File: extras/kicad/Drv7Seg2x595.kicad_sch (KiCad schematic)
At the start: 33 parts, among them IC1 74HC595, IC2 74HC595, J1 INTERFACE, J2 PWR_LED_JMP, Q1 MMBT3904, Q2 MMBT3904, Q3 MMBT3904, Q4 MMBT3904

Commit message: Update KiCAD files.
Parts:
- DISPLAY1: footprint Display_7Segment:CA56-12EWA -> Drv7Seg2x595:display_7seg_4d_0.56in
- J1: footprint Connector_PinHeader_2.54mm:PinHeader_1x05_P2.54mm_Horizontal -> Drv7Seg2x595:PinHeader_1x05_P2.54mm_Horizontal
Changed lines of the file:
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@@
 	)
 	(symbol
+		(lib_name "MountingHole_3")
 		(lib_id "Mechanical:MountingHole")
 		(at 234.95 102.87 0)
@@
 			)
 		)
-		(property "Footprint" "Display_7Segment:CA56-12EWA"
+		(property "Footprint" "Drv7Seg2x595:display_7seg_4d_0.56in"
 			(at 112.522 96.52 0)
 			(effects
@@
 			)
 		)
-		(property "Footprint" "Connector_PinHeader_2.54mm:PinHeader_1x05_P2.54mm_Horizontal"
+		(property "Footprint" "Drv7Seg2x595:PinHeader_1x05_P2.54mm_Horizontal"
 			(at 196.342 80.772 0)
 			(effects
@@
 	)
 	(symbol
+		(lib_name "MountingHole_2")
 		(lib_id "Mechanical:MountingHole")
 		(at 234.95 90.17 0)
@@
 	)
 	(symbol
+		(lib_name "MountingHole_1")
 		(lib_id "Mechanical:MountingHole")
 		(at 234.95 109.22 0)

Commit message: Add SOT-23 to project-wide library for portability.
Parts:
- Q3, Q4: footprint Package_TO_SOT_SMD:SOT-23 -> Drv7Seg2x595:SOT-23
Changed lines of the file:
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@@
 			)
 		)
-		(property "Footprint" "Package_TO_SOT_SMD:SOT-23"
+		(property "Footprint" "Drv7Seg2x595:SOT-23"
 			(at 128.27 95.885 0)
 			(effects
@@
 			)
 		)
-		(property "Footprint" "Package_TO_SOT_SMD:SOT-23"
+		(property "Footprint" "Drv7Seg2x595:SOT-23"
 			(at 116.84 104.775 0)
 			(effects

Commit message: Update symbol for transistors.
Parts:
- Q1, Q2: footprint Package_TO_SOT_SMD:SOT-23 -> Drv7Seg2x595:SOT-23; symbol Transistor_BJT:MMBT3904 -> Drv7Seg2x595:MMBT3904
- Q3, Q4: symbol Transistor_BJT:MMBT3904 -> Drv7Seg2x595:MMBT3904
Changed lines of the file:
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@@
 	)
 	(symbol
-		(lib_name "MMBT3904_1")
-		(lib_id "Transistor_BJT:MMBT3904")
+		(lib_id "Drv7Seg2x595:MMBT3904")
 		(at 133.35 93.98 0)
 		(mirror y)
@@
 	)
 	(symbol
-		(lib_id "Transistor_BJT:MMBT3904")
+		(lib_id "Drv7Seg2x595:MMBT3904")
 		(at 110.49 111.76 0)
 		(mirror y)
@@
 			)
 		)
-		(property "Footprint" "Package_TO_SOT_SMD:SOT-23"
+		(property "Footprint" "Drv7Seg2x595:SOT-23"
 			(at 105.41 113.665 0)
 			(effects
@@
 	)
 	(symbol
-		(lib_id "Transistor_BJT:MMBT3904")
+		(lib_id "Drv7Seg2x595:MMBT3904")
 		(at 99.06 120.65 0)
 		(mirror y)
@@
 			)
 		)
-		(property "Footprint" "Package_TO_SOT_SMD:SOT-23"
+		(property "Footprint" "Drv7Seg2x595:SOT-23"
 			(at 93.98 122.555 0)
 			(effects
@@
 	)
 	(symbol
-		(lib_id "Transistor_BJT:MMBT3904")
+		(lib_id "Drv7Seg2x595:MMBT3904")
 		(at 121.92 102.87 0)
 		(mirror y)

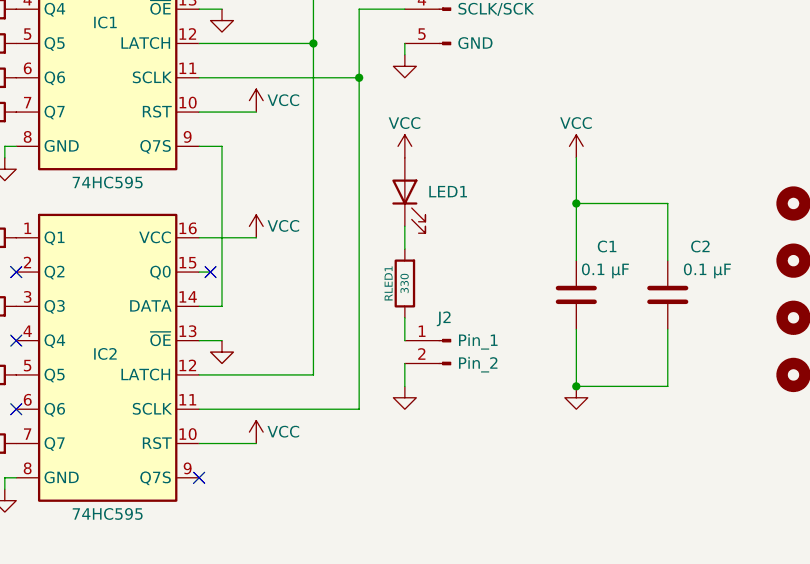
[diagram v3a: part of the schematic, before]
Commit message: Increase RLED1 value to 680 Ohm.
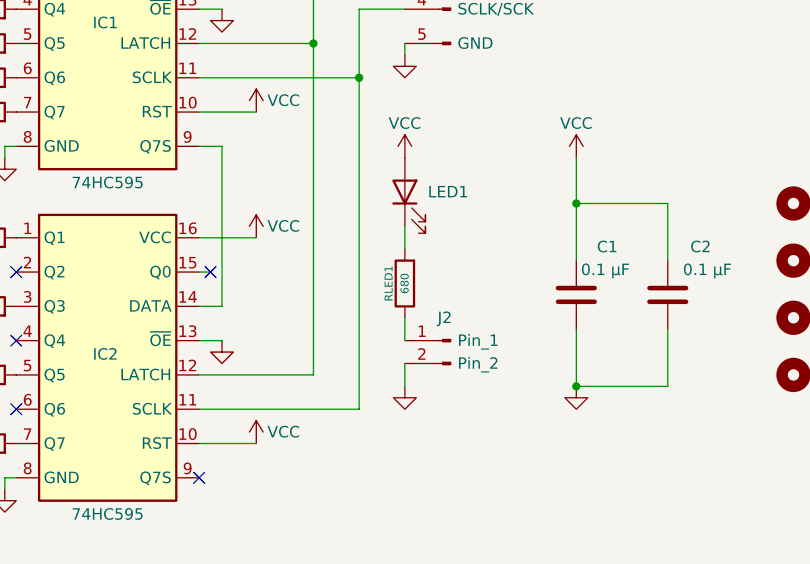
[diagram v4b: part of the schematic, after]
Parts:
- RLED1: value 330 -> 680
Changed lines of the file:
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@@
 			)
 		)
-		(property "Value" "330"
+		(property "Value" "680"
 			(at 191.77 99.06 90)
 			(effects

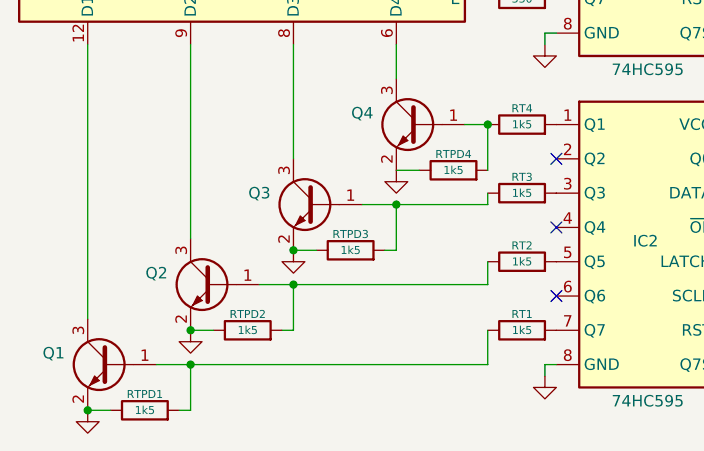
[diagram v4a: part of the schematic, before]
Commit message: Bump BJT base pull-down resistors values to 47k.
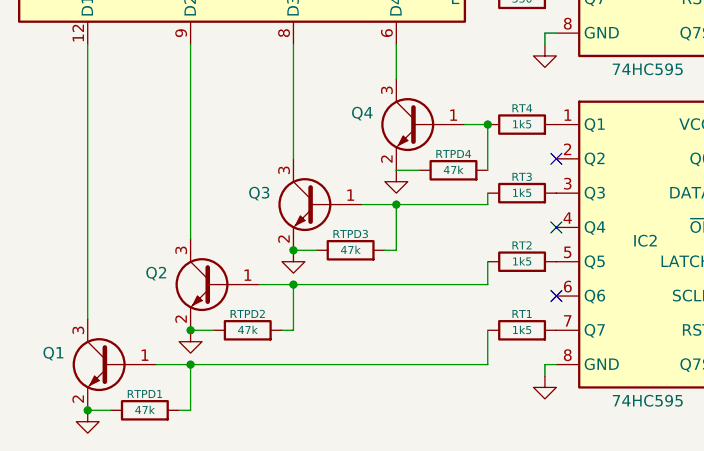
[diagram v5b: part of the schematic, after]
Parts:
- RTPD1, RTPD2, RTPD3, RTPD4: value 1k5 -> 47k
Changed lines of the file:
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@@
 			)
 		)
-		(property "Value" "1k5"
+		(property "Value" "47k"
 			(at 137.16 99.06 90)
 			(effects
@@
 			)
 		)
-		(property "Value" "1k5"
+		(property "Value" "47k"
 			(at 102.87 125.73 90)
 			(effects
@@
 			)
 		)
-		(property "Value" "1k5"
+		(property "Value" "47k"
 			(at 114.3 116.84 90)
 			(effects
@@
 			)
 		)
-		(property "Value" "1k5"
+		(property "Value" "47k"
 			(at 125.73 107.95 90)
 			(effects
